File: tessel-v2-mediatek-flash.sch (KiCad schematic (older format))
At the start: 0 parts

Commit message: adding flash
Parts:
- added C?: 0.1uF, symbol C
- added U?: S25FL256SAGNFI001, symbol S25FL256SAGNFI001
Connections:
- net labels added: +3V3, Flash_CS, Flash_HOLD, Flash_SCK, Flash_SI, Flash_SO, Flash_WP, GND
- wire segments 0 -> 12
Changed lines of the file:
@@
 Comment4 ""
 $EndDescr
+$Comp
+L S25FL256SAGNFI001 U?
+U 1 1 548FCC1A
+P 7800 4350
+F 0 "U?" H 7350 4700 60  0000 C CNN
+F 1 "S25FL256SAGNFI001" H 7800 4600 60  0000 C CNN
+F 2 "" H 7400 5350 60  0000 C CNN
+F 3 "" H 7400 5350 60  0000 C CNN
+	1    7800 4350
+	1    0    0    -1
+$EndComp
+Wire Wire Line
+	7100 4250 6750 4250
+Wire Wire Line
+	7100 4350 6750 4350
+Wire Wire Line
+	7100 4450 6750 4450
+Wire Wire Line
+	7100 4550 6750 4550
+Wire Wire Line
+	8500 4250 8950 4250
+Wire Wire Line
+	8500 4350 8950 4350
+Wire Wire Line
+	8500 4450 8950 4450
+Wire Wire Line
+	8500 4550 8950 4550
+Text Label 6750 4350 0    60   ~ 0
+Flash_CS
+Text Label 6750 4450 0    60   ~ 0
+Flash_SCK
+Text Label 8500 4250 0    60   ~ 0
+Flash_SI
+Text Label 8500 4350 0    60   ~ 0
+Flash_SO
+Text Label 8500 4450 0    60   ~ 0
+Flash_WP
+Text Label 8500 4550 0    60   ~ 0
+Flash_HOLD
+Text HLabel 8950 4250 2    60   Input ~ 0
+Flash_SI
+Text HLabel 8950 4350 2    60   Input ~ 0
+Flash_SO
+Text HLabel 8950 4450 2    60   Input ~ 0
+Flash_WP
+Text HLabel 8950 4550 2    60   Input ~ 0
+Flash_HOLD
+Text HLabel 6750 4350 0    60   Input ~ 0
+Flash_CS
+Text HLabel 6750 4450 0    60   Input ~ 0
+Flash_SCK
+$Comp
+L GND #PWR?
+U 1 1 548FCCD4
+P 6750 5650
+F 0 "#PWR?" H 6750 5400 60  0001 C CNN
+F 1 "GND" H 6750 5500 60  0000 C CNN
+F 2 "" H 6750 5650 60  0000 C CNN
+F 3 "" H 6750 5650 60  0000 C CNN
+	1    6750 5650
+	1    0    0    -1
+$EndComp
+Wire Wire Line
+	6750 4550 6750 5650
+$Comp
+L +3V3 #PWR?
+U 1 1 548FCD0C
+P 6750 4050
+F 0 "#PWR?" H 6750 3900 60  0001 C CNN
+F 1 "+3V3" H 6750 4190 60  0000 C CNN
+F 2 "" H 6750 4050 60  0000 C CNN
+F 3 "" H 6750 4050 60  0000 C CNN
+	1    6750 4050
+	1    0    0    -1
+$EndComp
+Wire Wire Line
+	6750 4250 6750 4050
+$Comp
+L C C?
+U 1 1 548FCD34
+P 7200 5250
+F 0 "C?" H 7200 5350 40  0000 L CNN
+F 1 "0.1uF" H 7206 5165 40  0000 L CNN
+F 2 "" H 7238 5100 30  0000 C CNN
+F 3 "" H 7200 5250 60  0000 C CNN
+	1    7200 5250
+	1    0    0    -1
+$EndComp
+Wire Wire Line
+	7200 5450 6750 5450
+Connection ~ 6750 5450
+$Comp
+L +3V3 #PWR?
+U 1 1 548FCD90
+P 7200 4950
+F 0 "#PWR?" H 7200 4800 60  0001 C CNN
+F 1 "+3V3" H 7200 5090 60  0000 C CNN
+F 2 "" H 7200 4950 60  0000 C CNN
+F 3 "" H 7200 4950 60  0000 C CNN
+	1    7200 4950
+	1    0    0    -1
+$EndComp
+Wire Wire Line
+	7200 5050 7200 4950
 $EndSCHEMATC

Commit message: swapped in power labels
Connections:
- net labels added: +3.3V
- net labels removed: +3V3
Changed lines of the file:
@@
 	6750 4550 6750 5650
 $Comp
-L +3V3 #PWR?
+L +3.3V #PWR?
 U 1 1 548FCD0C
 P 6750 4050
 F 0 "#PWR?" H 6750 3900 60  0001 C CNN
-F 1 "+3V3" H 6750 4190 60  0000 C CNN
+F 1 "+3.3V" H 6750 4190 60  0000 C CNN
 F 2 "" H 6750 4050 60  0000 C CNN
 F 3 "" H 6750 4050 60  0000 C CNN
@@
 Connection ~ 6750 5450
 $Comp
-L +3V3 #PWR?
+L +3.3V #PWR?
 U 1 1 548FCD90
 P 7200 4950
 F 0 "#PWR?" H 7200 4800 60  0001 C CNN
-F 1 "+3V3" H 7200 5090 60  0000 C CNN
+F 1 "+3.3V" H 7200 5090 60  0000 C CNN
 F 2 "" H 7200 4950 60  0000 C CNN
 F 3 "" H 7200 4950 60  0000 C CNN

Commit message: annotated
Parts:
- gave numbers to parts that had none: 2
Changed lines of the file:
@@
 $EndDescr
 $Comp
-L S25FL256SAGNFI001 U?
+L S25FL256SAGNFI001 U401
 U 1 1 548FCC1A
 P 7800 4350
-F 0 "U?" H 7350 4700 60  0000 C CNN
+F 0 "U401" H 7350 4700 60  0000 C CNN
 F 1 "S25FL256SAGNFI001" H 7800 4600 60  0000 C CNN
 F 2 "" H 7400 5350 60  0000 C CNN
@@
 Flash_SCK
 $Comp
-L GND #PWR?
+L GND #PWR402
 U 1 1 548FCCD4
 P 6750 5650
-F 0 "#PWR?" H 6750 5400 60  0001 C CNN
+F 0 "#PWR402" H 6750 5400 60  0001 C CNN
 F 1 "GND" H 6750 5500 60  0000 C CNN
 F 2 "" H 6750 5650 60  0000 C CNN
@@
 	6750 4550 6750 5650
 $Comp
-L +3.3V #PWR?
+L +3.3V #PWR401
 U 1 1 548FCD0C
 P 6750 4050
-F 0 "#PWR?" H 6750 3900 60  0001 C CNN
+F 0 "#PWR401" H 6750 3900 60  0001 C CNN
 F 1 "+3.3V" H 6750 4190 60  0000 C CNN
 F 2 "" H 6750 4050 60  0000 C CNN
@@
 	6750 4250 6750 4050
 $Comp
-L C C?
+L C C401
 U 1 1 548FCD34
 P 7200 5250
-F 0 "C?" H 7200 5350 40  0000 L CNN
+F 0 "C401" H 7200 5350 40  0000 L CNN
 F 1 "0.1uF" H 7206 5165 40  0000 L CNN
 F 2 "" H 7238 5100 30  0000 C CNN
@@
 Connection ~ 6750 5450
 $Comp
-L +3.3V #PWR?
+L +3.3V #PWR403
 U 1 1 548FCD90
 P 7200 4950
-F 0 "#PWR?" H 7200 4800 60  0001 C CNN
+F 0 "#PWR403" H 7200 4800 60  0001 C CNN
 F 1 "+3.3V" H 7200 5090 60  0000 C CNN
 F 2 "" H 7200 4950 60  0000 C CNN

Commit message: give nF some love
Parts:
- C401: value 0.1uF -> 100nF
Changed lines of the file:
@@
 P 7200 5250
 F 0 "C401" H 7200 5350 40  0000 L CNN
-F 1 "0.1uF" H 7206 5165 40  0000 L CNN
+F 1 "100nF" H 7206 5165 40  0000 L CNN
 F 2 "" H 7238 5100 30  0000 C CNN
 F 3 "" H 7200 5250 60  0000 C CNN

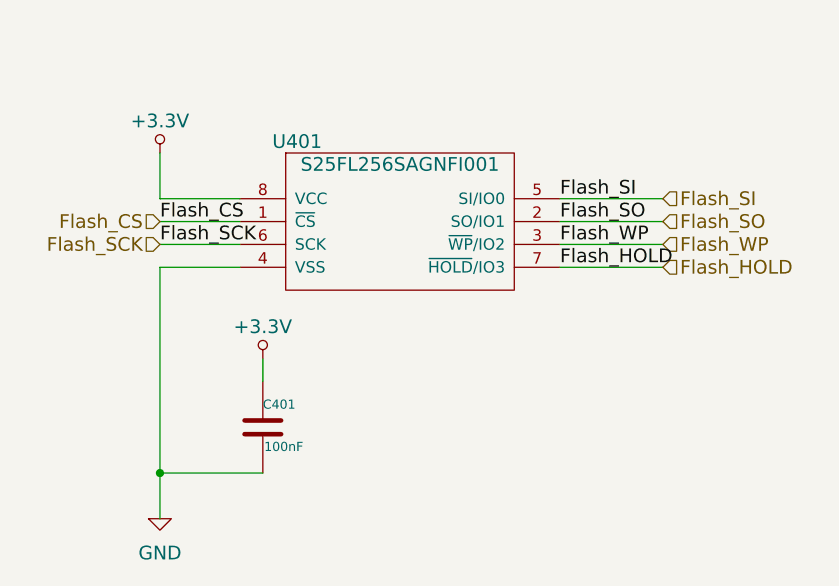
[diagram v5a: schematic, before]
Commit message: TIL: hlabel, llabel share a namespace
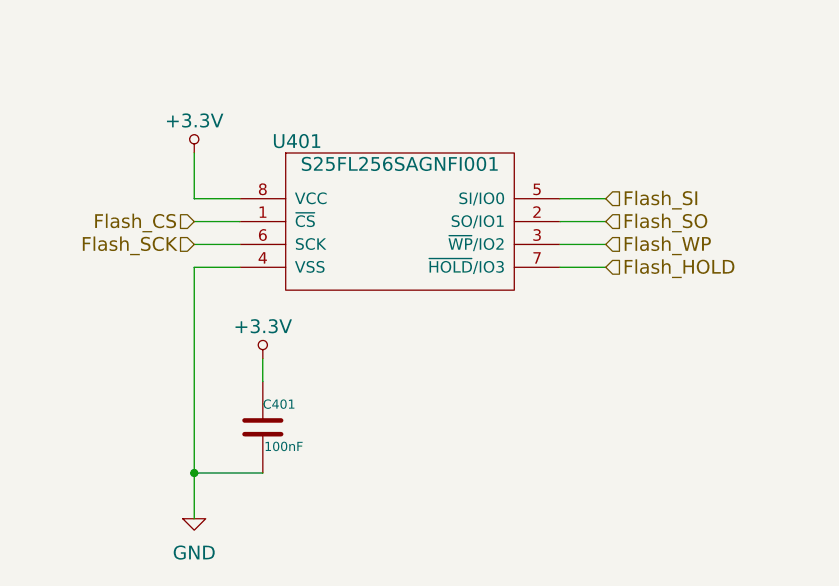
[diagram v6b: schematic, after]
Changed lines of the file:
@@
 $EndComp
 Wire Wire Line
-	7100 4250 6750 4250
+	7100 4250 6900 4250
 Wire Wire Line
-	7100 4350 6750 4350
+	7100 4350 6900 4350
 Wire Wire Line
-	7100 4450 6750 4450
+	7100 4450 6900 4450
 Wire Wire Line
-	7100 4550 6750 4550
+	7100 4550 6900 4550
 Wire Wire Line
-	8500 4250 8950 4250
+	8500 4250 8700 4250
 Wire Wire Line
-	8500 4350 8950 4350
+	8500 4350 8700 4350
 Wire Wire Line
-	8500 4450 8950 4450
+	8500 4450 8700 4450
 Wire Wire Line
-	8500 4550 8950 4550
-Text Label 6750 4350 0    60   ~ 0
+	8500 4550 8700 4550
+Text HLabel 8700 4250 2    60   Input ~ 0
+Flash_SI
+Text HLabel 8700 4350 2    60   Input ~ 0
+Flash_SO
+Text HLabel 8700 4450 2    60   Input ~ 0
+Flash_WP
+Text HLabel 8700 4550 2    60   Input ~ 0
+Flash_HOLD
+Text HLabel 6900 4350 0    60   Input ~ 0
 Flash_CS
-Text Label 6750 4450 0    60   ~ 0
-Flash_SCK
-Text Label 8500 4250 0    60   ~ 0
-Flash_SI
-Text Label 8500 4350 0    60   ~ 0
-Flash_SO
-Text Label 8500 4450 0    60   ~ 0
-Flash_WP
-Text Label 8500 4550 0    60   ~ 0
-Flash_HOLD
-Text HLabel 8950 4250 2    60   Input ~ 0
-Flash_SI
-Text HLabel 8950 4350 2    60   Input ~ 0
-Flash_SO
-Text HLabel 8950 4450 2    60   Input ~ 0
-Flash_WP
-Text HLabel 8950 4550 2    60   Input ~ 0
-Flash_HOLD
-Text HLabel 6750 4350 0    60   Input ~ 0
-Flash_CS
-Text HLabel 6750 4450 0    60   Input ~ 0
+Text HLabel 6900 4450 0    60   Input ~ 0
 Flash_SCK
 $Comp
 L GND #PWR024
 U 1 1 548FCCD4
-P 6750 5650
-F 0 "#PWR024" H 6750 5400 60  0001 C CNN
-F 1 "GND" H 6750 5500 60  0000 C CNN
-F 2 "" H 6750 5650 60  0000 C CNN
-F 3 "" H 6750 5650 60  0000 C CNN
-	1    6750 5650
+P 6900 5650
+F 0 "#PWR024" H 6900 5400 60  0001 C CNN
+F 1 "GND" H 6900 5500 60  0000 C CNN
+F 2 "" H 6900 5650 60  0000 C CNN
+F 3 "" H 6900 5650 60  0000 C CNN
+	1    6900 5650
 	1    0    0    -1
 $EndComp
 Wire Wire Line
-	6750 4550 6750 5650
+	6900 4550 6900 5450
+Wire Wire Line
+	6900 5450 6900 5650
 $Comp
 L +3.3V #PWR025
 U 1 1 548FCD0C
-P 6750 4050
-F 0 "#PWR025" H 6750 3900 60  0001 C CNN
-F 1 "+3.3V" H 6750 4190 60  0000 C CNN
-F 2 "" H 6750 4050 60  0000 C CNN
-F 3 "" H 6750 4050 60  0000 C CNN
-	1    6750 4050
+P 6900 4050
+F 0 "#PWR025" H 6900 3900 60  0001 C CNN
+F 1 "+3.3V" H 6900 4190 60  0000 C CNN
+F 2 "" H 6900 4050 60  0000 C CNN
+F 3 "" H 6900 4050 60  0000 C CNN
+	1    6900 4050
 	1    0    0    -1
 $EndComp
 Wire Wire Line
-	6750 4250 6750 4050
+	6900 4250 6900 4050
 $Comp
 L C C401
@@
 $EndComp
 Wire Wire Line
-	7200 5450 6750 5450
-Connection ~ 6750 5450
+	7200 5450 6900 5450
+Connection ~ 6900 5450
 $Comp
 L +3.3V #PWR026

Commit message: TIL: -am...but also P-->J
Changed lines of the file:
@@
 Flash_SCK
 $Comp
-L GND #PWR024
+L GND #PWR402
 U 1 1 548FCCD4
 P 6900 5650
-F 0 "#PWR024" H 6900 5400 60  0001 C CNN
+F 0 "#PWR402" H 6900 5400 60  0001 C CNN
 F 1 "GND" H 6900 5500 60  0000 C CNN
 F 2 "" H 6900 5650 60  0000 C CNN
@@
 $EndComp
 Wire Wire Line
-	6900 4550 6900 5450
-Wire Wire Line
-	6900 5450 6900 5650
+	6900 4550 6900 5650
 $Comp
-L +3.3V #PWR025
+L +3.3V #PWR401
 U 1 1 548FCD0C
 P 6900 4050
-F 0 "#PWR025" H 6900 3900 60  0001 C CNN
+F 0 "#PWR401" H 6900 3900 60  0001 C CNN
 F 1 "+3.3V" H 6900 4190 60  0000 C CNN
 F 2 "" H 6900 4050 60  0000 C CNN
@@
 Connection ~ 6900 5450
 $Comp
-L +3.3V #PWR026
+L +3.3V #PWR403
 U 1 1 548FCD90
 P 7200 4950
-F 0 "#PWR026" H 7200 4800 60  0001 C CNN
+F 0 "#PWR403" H 7200 4800 60  0001 C CNN
 F 1 "+3.3V" H 7200 5090 60  0000 C CNN
 F 2 "" H 7200 4950 60  0000 C CNN
